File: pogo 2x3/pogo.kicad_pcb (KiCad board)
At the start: 2 copper layers, 15.2 x 19.6 mm, 2 parts, among them J1 AVR-ISP-6, J2 PinHeader_1x06_P2.54mm_Horizo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

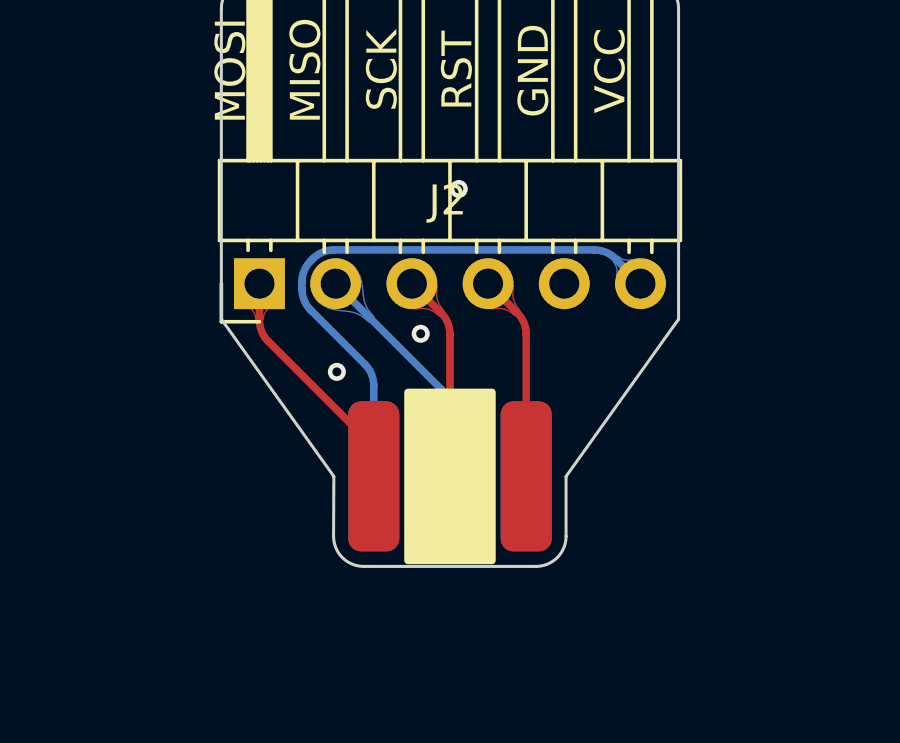
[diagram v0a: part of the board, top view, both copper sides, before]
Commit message: fixed pogo and dip adapter
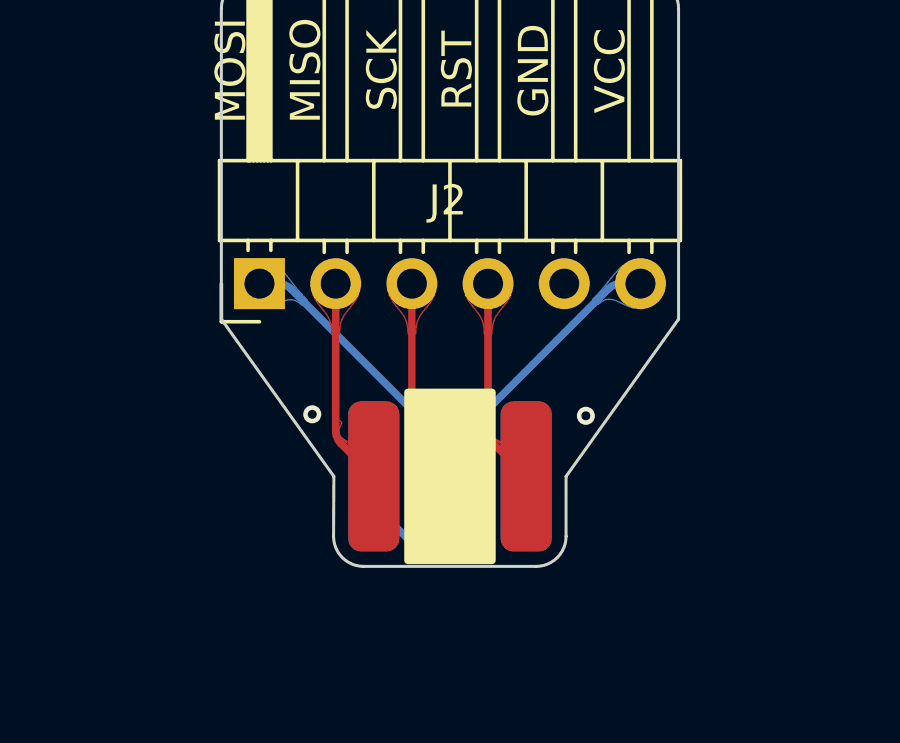
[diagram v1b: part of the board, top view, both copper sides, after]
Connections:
- J1 pad 1: MOSI -> MISO
- J1 pad 4: MISO -> MOSI
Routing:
- net +5V: track 19.7 -> 16.8 mm
- net MOSI: track 7.91 -> 9.51 mm
- net MISO: track 7.96 -> 6.92 mm
- net GND: vias 3 -> 2
